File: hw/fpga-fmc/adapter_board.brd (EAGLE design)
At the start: 69 x 84 mm, 176 parts, among them IC1 M24C02, J1 5569262-1, J2 ASP-134488-01, U1 ADM3066E, U10 ADM3066E, U11 ADM3066E, U12 ADM3066E, U13 ADM3066E, U14 ADM3066E, U15 ADM3066E, U16 ADM3066E, U17 TCA9548A, U18 TXS0102, U19 TXS0102, U2 ADM3066E, U20 TXS0102, U21 TXS0102, U3 ADM3066E, U4 ADM3066E, U40 IRLML2502, U5 ADM3066E, U6 ADM3066E, U7 ADM3066E, U8 ADM3066E, U9 ADM3066E

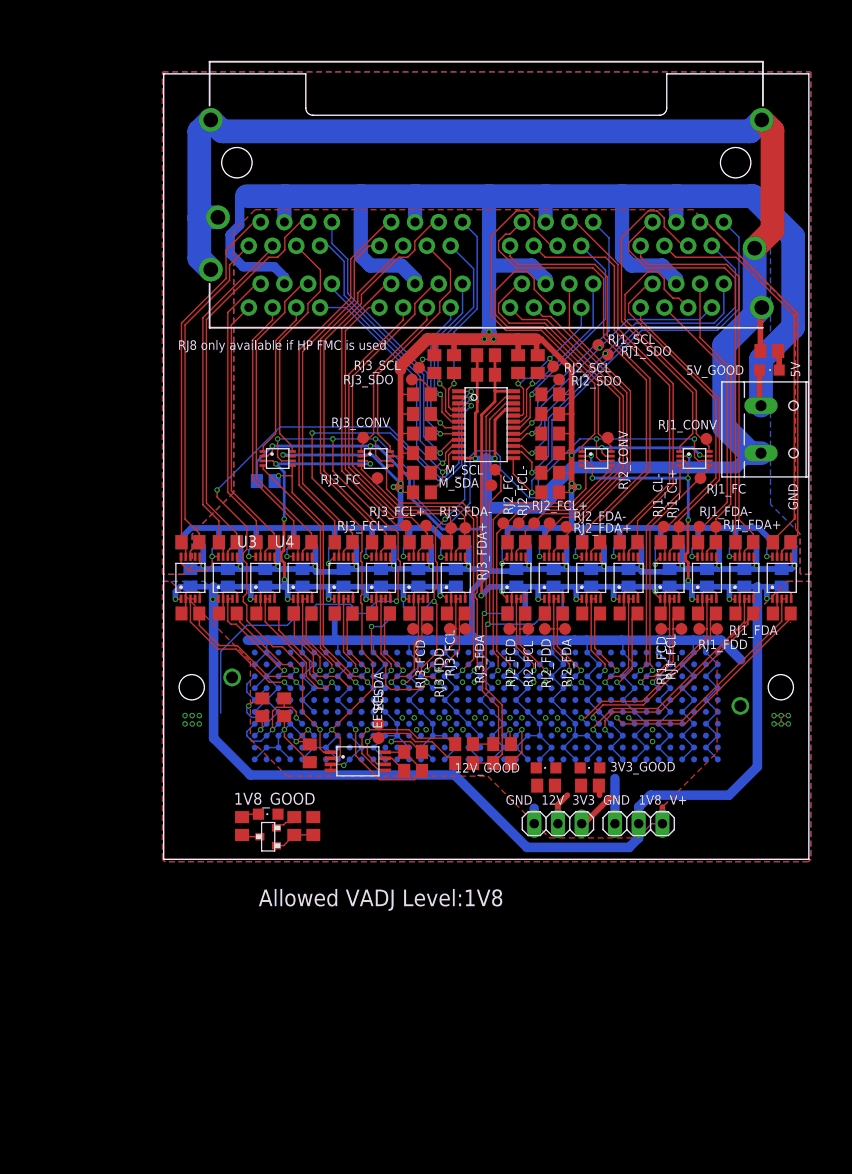
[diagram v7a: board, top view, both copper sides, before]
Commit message: hw/fpga-fmc: rewire pin header and screw terminal.
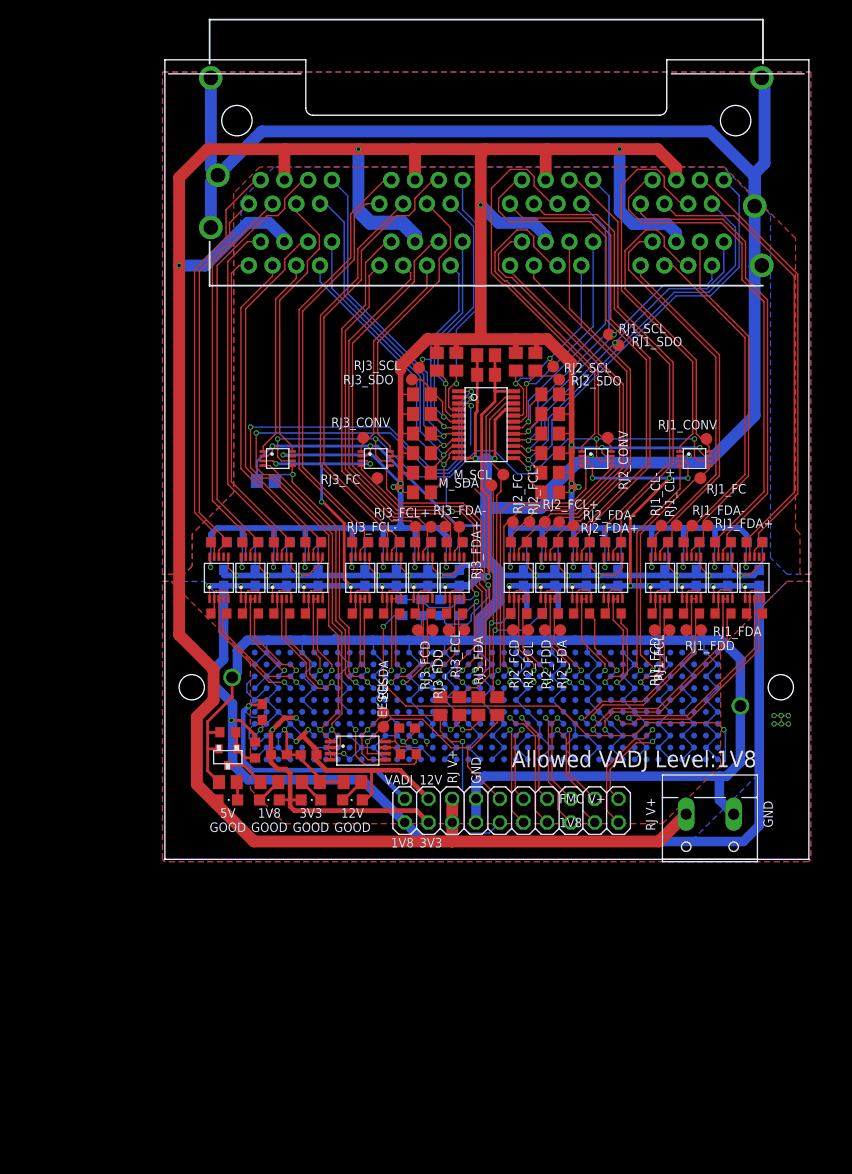
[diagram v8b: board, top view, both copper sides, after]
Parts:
- removed J3, J4: (no value), pinhead:1X03
- added JP1: (no value), pinhead:2X10
- C1, C10, C11, C12, C13, C14, C15, C16, C17, C18, C19, C2, C20, C21, C22, C23, C24, C25, C26, C27, C28, C29, C30, C31, C32, C33, C34, C35, C36, C37, C39, C5, C6, C7, C8, C9: device rcl:C0805 -> rcl:C0603
- R1, R2, R22, R23, R24, R25, R26, R27, R28, R29, R30, R31, R32, R33, R34, R35, R36, R37, R38, R39, R40, R41, R42, R43, R44, R45, R46, R47, R48, R49, R5, R50, R51, R52, R55, R57, R58, R6, R7: device rcl:R0805 -> rcl:R0603
- R60, R61: device resistor:R0805 -> resistor:R0603
- moved R53 74.0 mm to (6.86, 8.26)
- moved 5V_GOOD 73.9 mm to (6.86, 6.35)
- moved X1 42.2 mm to (58.4, 4.19), turned to 180 degrees
- moved 3V3_GOOD 30.0 mm to (15.7, 6.35), turned to 270 degrees
- moved R56 29.8 mm to (15.7, 8.26)
- moved 12V_GOOD 21.0 mm to (20.2, 6.35)
- moved R54 20.7 mm to (20.2, 8.26), turned to 0 degrees
- moved R61 12.3 mm to (6.86, 13.6), turned to 180 degrees
- moved R58 10.7 mm to (25.5, 26.9), turned to 90 degrees
- moved R60 10.2 mm to (9.78, 11.7)
- moved U40 9.54 mm to (6.86, 10.9), turned to 180 degrees
- moved R57 8.41 mm to (31.6, 26.9), turned to 270 degrees
- moved R55 8.34 mm to (27.6, 26.9), turned to 90 degrees
- moved R64 7.06 mm to (35.7, 16.4), turned to 90 degrees
- moved R66 6.60 mm to (33.7, 16.4), turned to 270 degrees
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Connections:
- net +12V: now also JP1.4; no longer J3.2
- net +3V3: now also JP1.3; no longer J3.1
- net 0V: now also JP1.7, JP1.8, X1.1; no longer J3.3, J4.3, X1.2
- net 1V8: now also JP1.1; no longer J4.2
- net 5V: now also JP1.5, JP1.6, X1.2; no longer X1.1
- net FMC_DP0_M2C_N: now also JP1.19
- net FMC_DP0_M2C_P: now also JP1.20
- net FMC_IIC_SCL: now also JP1.10
- net FMC_IIC_SDA: now also JP1.9
- net FMC_LA09_N: now also JP1.15
- net FMC_LA09_P: now also JP1.16
- net FMC_LA10_N: now also JP1.17
- net FMC_LA10_P: now also JP1.18
- net FMC_LA13_N: now also JP1.13
- net FMC_LA13_P: now also JP1.14
- net FMC_LA14_N: now also JP1.11; no longer R65.2
- net FMC_LA14_P: now also JP1.12; no longer R66.2
- net FMC_LA20_N: now also R57.2
- net FMC_LA20_P: now also R7.1, U17.P2
- net FMC_LA22_N: no longer R57.2
- net FMC_LA22_P: no longer R7.1, U17.P2
- net FMC_LA23_N: now also R65.2
- net FMC_LA23_P: now also R66.2
- net V+: now also JP1.2; no longer J4.1
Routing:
- net 5V: track 408.6 -> 525.1 mm, vias 28 -> 30
- net 0V: track 734.6 -> 811.0 mm, vias 38 -> 28
- net FMC_LA20_P: track 0.00 -> 37.2 mm, vias 0 -> 3
- net 1V8_POWER_GOOD: track 16.4 -> 53.4 mm, vias 0 -> 2
- net FMC_LA22_P: track 37.5 -> 0.90 mm, vias 4 -> 1
- net V+: track 12.9 -> 35.5 mm
- net CONV_OE: track 109.1 -> 87.9 mm
- net +3V3: track 17.6 -> 37.5 mm
- net FMC_IIC_SDA: track 17.5 -> 33.6 mm, vias 1 -> 2
- net +12V: track 8.63 -> 24.4 mm
- net FMC_LA22_N: track 15.7 -> 0.90 mm, vias 2 -> 1
- net FMC_LA13_N: track 0.00 -> 14.2 mm, vias 0 -> 1
- net FMC_DP0_M2C_N: track 0.00 -> 13.9 mm, vias 0 -> 1
- net FMC_LA09_N: track 0.00 -> 13.2 mm, vias 0 -> 1
- net FMC_LA20_N: track 0.00 -> 13.1 mm, vias 0 -> 2
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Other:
- board size 69 x 84 mm -> 68.9 x 85.5 mm
- board text added: "12V GOOD"
- board text added: "1V8 GOOD"
- board text added: "3V3 GOOD"
- board text added: "5V GOOD"
- board text added: "FMC V+"
- board text added: "RJ V+"
- board text added: "VADJ"
- board text removed: "5V"
- board text removed: "RJ8 only available if HP FMC is used"
- board text removed: "V+"
